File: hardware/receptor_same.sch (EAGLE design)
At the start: 62 parts, among them J1 ICSP, J2 SERIAL, J3 GPIO, J4 AUX-POWER, K1 HLS8L-DC5V, Q1 MMBT3904LT1G, U1 ATMEGA328P_TQFP, U2 SI4707, U3 TPA6111A2DR, U4 MCP16301/H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

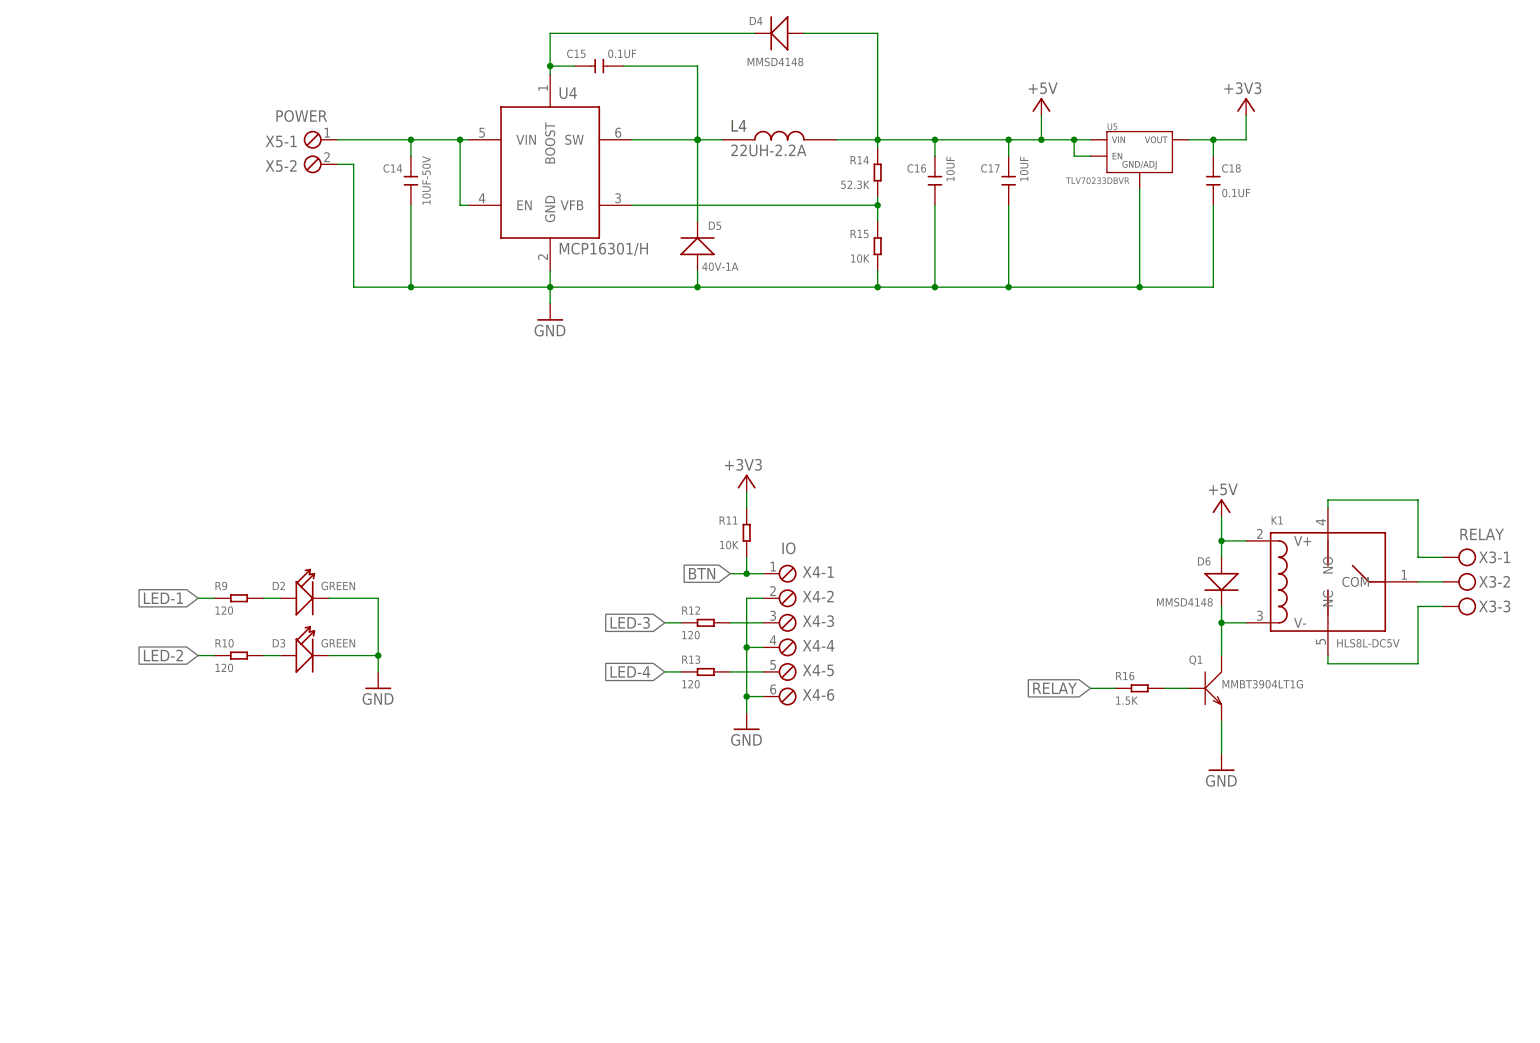
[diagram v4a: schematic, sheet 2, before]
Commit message: puntos de montaje en esquematico y pasa el erc
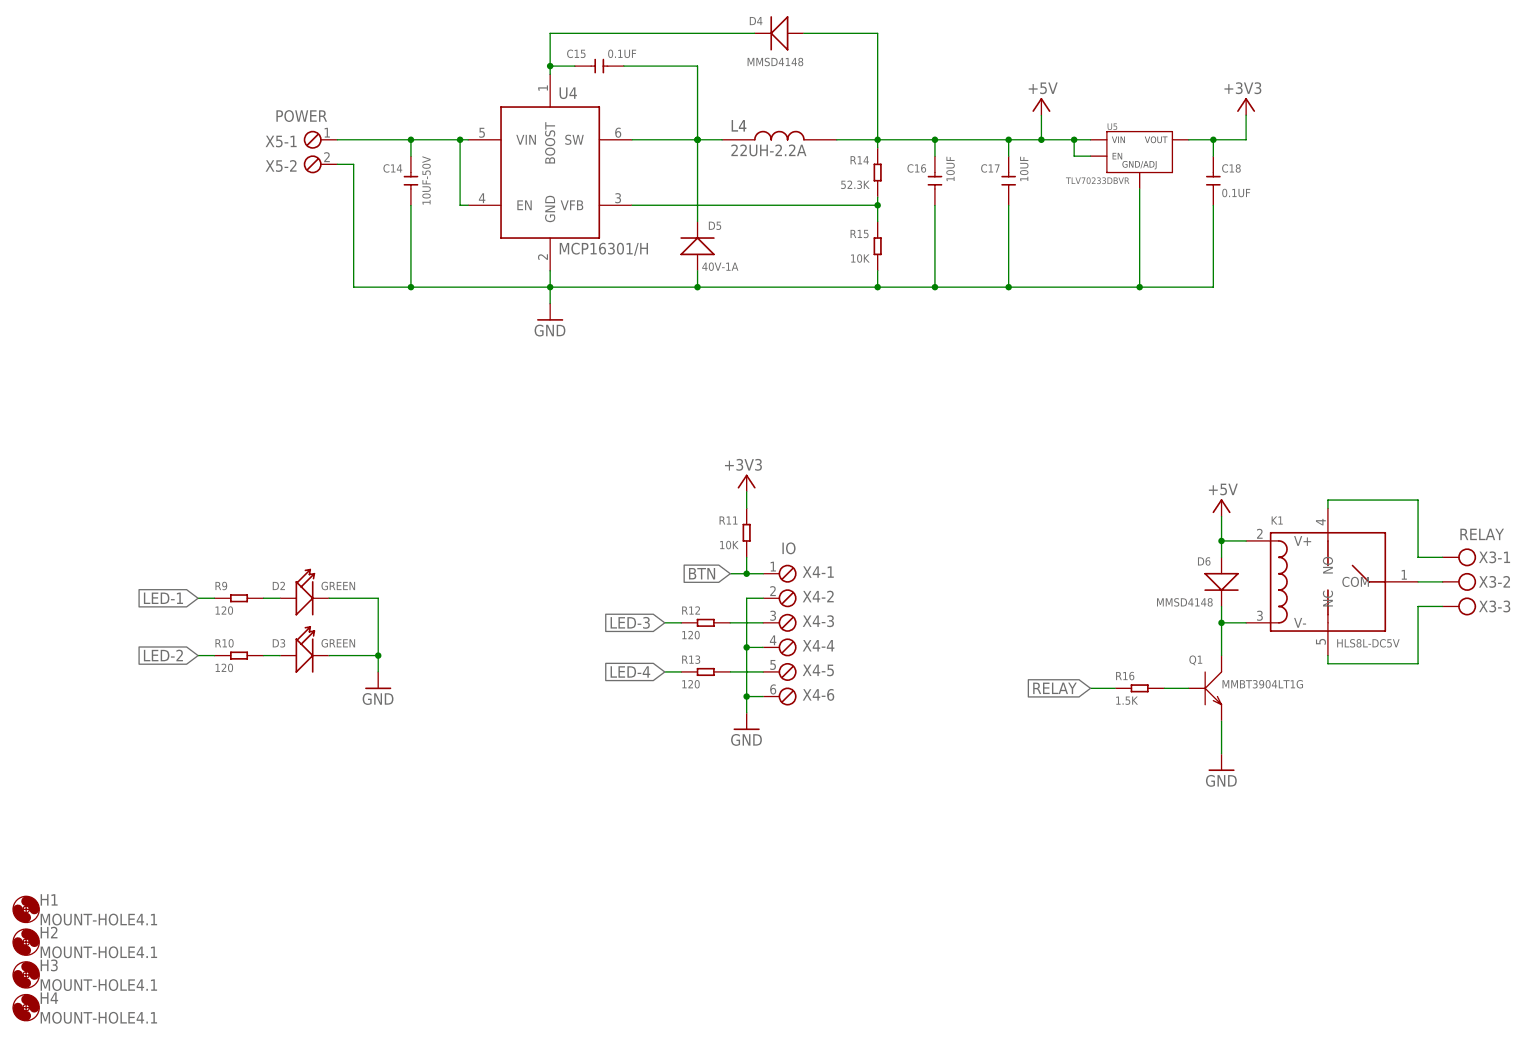
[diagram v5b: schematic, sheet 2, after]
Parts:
- added H1, H2, H3, H4: MOUNT-HOLE4.1, holes:MOUNT-HOLE4.1
- X1: value ANTENNA -> ANT
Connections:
- net N$23 renamed SW
- net N$25 renamed VIN
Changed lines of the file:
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@@
 </classes>
 <parts>
-<part name="FRAME1" library="frames" library_urn="urn:adsk.eagle:library:229" deviceset="A4L-LOC" device=""/>
+<part name="FRAME1" library="frames" library_urn="urn:adsk.eagle:library:229" deviceset="A4L-LOC" device="" value="SHEET-1"/>
 <part name="U1" library="SparkFun-IC-Microcontroller" library_urn="urn:adsk.eagle:library:525" deviceset="ATMEGA328P_TQFP" device="" package3d_urn="urn:adsk.eagle:package:38945/1" value="ATMEGA328P_TQFP">
 <attribute name="MPN" value="ATMEGA328P-AU"/>
@@
 <attribute name="SPICEPREFIX" value="G"/>
 </part>
-<part name="P+9" library="supply1" library_urn="urn:adsk.eagle:library:371" deviceset="VCC" device=""/>
 <part name="GND11" library="supply1" library_urn="urn:adsk.eagle:library:371" deviceset="GND" device="">
 <attribute name="SPICEPREFIX" value="G"/>
@@
 <part name="P+11" library="supply1" library_urn="urn:adsk.eagle:library:371" deviceset="+3V3" device=""/>
 <part name="GND17" library="supply1" library_urn="urn:adsk.eagle:library:371" deviceset="GND" device=""/>
-<part name="X1" library="con-phoenix-254" library_urn="urn:adsk.eagle:library:172" deviceset="MPT2" device="" package3d_urn="urn:adsk.eagle:package:9320/1" value="ANTENNA">
+<part name="X1" library="con-phoenix-254" library_urn="urn:adsk.eagle:library:172" deviceset="MPT2" device="" package3d_urn="urn:adsk.eagle:package:9320/1" value="ANT">
 <attribute name="MPN" value="1725656"/>
 </part>
@@
 <attribute name="MPN" value="RC0805JR-07120RL"/>
 </part>
-<part name="FRAME2" library="frames" library_urn="urn:adsk.eagle:library:229" deviceset="A4L-LOC" device=""/>
+<part name="FRAME2" library="frames" library_urn="urn:adsk.eagle:library:229" deviceset="A4L-LOC" device="" value="SHEET-2"/>
 <part name="K1" library="OPL_Relay" library_urn="urn:adsk.eagle:library:8004835" deviceset="RELAY-HLS8L-DC5V-S-C" device="HLS8L-DC5V-S-C" package3d_urn="urn:adsk.eagle:package:8004880/1" value="HLS8L-DC5V">
 <attribute name="MPN" value="HLS8L-DC5V-S-C"/>
@@
 <part name="P+19" library="supply1" library_urn="urn:adsk.eagle:library:371" deviceset="+3V3" device=""/>
 <part name="R15" library="OPL_Resistor" library_urn="urn:adsk.eagle:library:8004883" deviceset="SMD-RES-10K-5%-1/10W(0603)" device="" package3d_urn="urn:adsk.eagle:package:8004941/1" value="10K"/>
+<part name="H1" library="holes" library_urn="urn:adsk.eagle:library:237" deviceset="MOUNT-HOLE" device="4.1" package3d_urn="urn:adsk.eagle:package:14273/1"/>
+<part name="H2" library="holes" library_urn="urn:adsk.eagle:library:237" deviceset="MOUNT-HOLE" device="4.1" package3d_urn="urn:adsk.eagle:package:14273/1"/>
+<part name="H3" library="holes" library_urn="urn:adsk.eagle:library:237" deviceset="MOUNT-HOLE" device="4.1" package3d_urn="urn:adsk.eagle:package:14273/1"/>
+<part name="H4" library="holes" library_urn="urn:adsk.eagle:library:237" deviceset="MOUNT-HOLE" device="4.1" package3d_urn="urn:adsk.eagle:package:14273/1"/>
+<part name="P+20" library="supply1" library_urn="urn:adsk.eagle:library:371" deviceset="+3V3" device=""/>
 </parts>
 <sheets>
@@
 <attribute name="VALUE" x="220.98" y="106.68" size="1.778" layer="96"/>
 </instance>
-<instance part="P+9" gate="VCC" x="176.53" y="76.2" smashed="yes">
-<attribute name="VALUE" x="179.07" y="78.74" size="1.778" layer="96" rot="R180"/>
-</instance>
 <instance part="GND11" gate="1" x="176.53" y="49.53" smashed="yes">
 <attribute name="VALUE" x="173.99" y="46.99" size="1.778" layer="96"/>
@@
 <instance part="P+18" gate="1" x="58.42" y="123.19" smashed="yes">
 <attribute name="VALUE" x="60.96" y="125.73" size="1.778" layer="96" rot="R180"/>
+</instance>
+<instance part="P+20" gate="G$1" x="176.53" y="74.93" smashed="yes">
+<attribute name="VALUE" x="179.07" y="77.47" size="1.778" layer="96" rot="R180"/>
 </instance>
 </instances>
@@
 <pinref part="U3" gate="G$1" pin="VDD"/>
 <wire x1="179.07" y1="67.31" x2="176.53" y2="67.31" width="0.1524" layer="91"/>
-<pinref part="P+9" gate="VCC" pin="VCC"/>
-<wire x1="176.53" y1="67.31" x2="176.53" y2="73.66" width="0.1524" layer="91"/>
+<wire x1="176.53" y1="67.31" x2="176.53" y2="72.39" width="0.1524" layer="91"/>
+<pinref part="P+20" gate="G$1" pin="+3V3"/>
 </segment>
 <segment>
@@
 <attribute name="NAME" x="146.05" y="133.35" size="1.27" layer="95" ratio="10" rot="R180"/>
 <attribute name="VALUE" x="146.05" y="129.54" size="1.27" layer="96" ratio="10" rot="R180"/>
+</instance>
+<instance part="H1" gate="G$1" x="15.24" y="27.94" smashed="yes">
+<attribute name="NAME" x="17.272" y="28.5242" size="1.778" layer="95"/>
+<attribute name="VALUE" x="17.272" y="25.4762" size="1.778" layer="96"/>
+</instance>
+<instance part="H2" gate="G$1" x="15.24" y="22.86" smashed="yes">
+<attribute name="NAME" x="17.272" y="23.4442" size="1.778" layer="95"/>
+<attribute name="VALUE" x="17.272" y="20.3962" size="1.778" layer="96"/>
+</instance>
+<instance part="H3" gate="G$1" x="15.24" y="17.78" smashed="yes">
+<attribute name="NAME" x="17.272" y="18.3642" size="1.778" layer="95"/>
+<attribute name="VALUE" x="17.272" y="15.3162" size="1.778" layer="96"/>
+</instance>
+<instance part="H4" gate="G$1" x="15.24" y="12.7" smashed="yes">
+<attribute name="NAME" x="17.272" y="13.2842" size="1.778" layer="95"/>
+<attribute name="VALUE" x="17.272" y="10.2362" size="1.778" layer="96"/>
 </instance>
 </instances>
@@
 </segment>
 </net>
-<net name="N$25" class="0">
+<net name="VIN" class="0">
 <segment>
 <wire x1="83.82" y1="137.16" x2="82.55" y2="137.16" width="0.1524" layer="91"/>
@@
 </segment>
 </net>
-<net name="N$23" class="0">
-<segment>
-<wire x1="109.22" y1="147.32" x2="119.38" y2="147.32" width="0.1524" layer="91"/>
+<net name="SW" class="0">
+<segment>
 <wire x1="119.38" y1="147.32" x2="119.38" y2="158.75" width="0.1524" layer="91"/>
 <pinref part="C15" gate="G$1" pin="1"/>
@@
 <wire x1="119.38" y1="147.32" x2="123.19" y2="147.32" width="0.1524" layer="91"/>
 <junction x="119.38" y="147.32"/>
+<wire x1="119.38" y1="134.62" x2="119.38" y2="147.32" width="0.1524" layer="91"/>
 <pinref part="U4" gate="G$1" pin="SW"/>
-<wire x1="119.38" y1="134.62" x2="119.38" y2="147.32" width="0.1524" layer="91"/>
-</segment>
-</net>
+<wire x1="119.38" y1="147.32" x2="109.22" y2="147.32" width="0.1524" layer="91"/>
+</segment>
+</net>

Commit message: avances ruteo si + amp
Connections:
- net N$11: now also C10.+; no longer C9.+
- net N$13: now also C9.+; no longer C10.+
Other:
- moved on the sheet: C10, C9, L2, L3, X2-1, X2-2, X2-3
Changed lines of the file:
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@@
 <setting verticaltext="up"/>
 </settings>
-<grid distance="0.1" unitdist="inch" unit="inch" style="lines" multiple="1" display="no" altdistance="0.01" altunitdist="inch" altunit="inch"/>
+<grid distance="0.05" unitdist="inch" unit="inch" style="lines" multiple="1" display="no" altdistance="0.01" altunitdist="inch" altunit="inch"/>
 <layers>
 <layer number="1" name="Top" color="4" fill="1" visible="no" active="no"/>
@@
 <attribute name="VALUE" x="181.61" y="83.82" size="1.27" layer="96" ratio="10"/>
 </instance>
-<instance part="C9" gate="G$1" x="212.09" y="69.85" smashed="yes" rot="R90">
-<attribute name="NAME" x="211.455" y="72.136" size="1.778" layer="95" font="vector" rot="R180"/>
-<attribute name="VALUE" x="220.091" y="68.326" size="1.778" layer="96" font="vector" rot="R180"/>
-<attribute name="MPN" x="212.09" y="69.85" size="1.778" layer="96" rot="R90" display="off"/>
-</instance>
-<instance part="C10" gate="G$1" x="212.09" y="62.23" smashed="yes" rot="R90">
-<attribute name="NAME" x="211.455" y="64.516" size="1.778" layer="95" font="vector" rot="R180"/>
-<attribute name="VALUE" x="220.091" y="60.706" size="1.778" layer="96" font="vector" rot="R180"/>
-<attribute name="MPN" x="212.09" y="62.23" size="1.778" layer="96" rot="R90" display="off"/>
-</instance>
-<instance part="L2" gate="L" x="226.06" y="69.85" smashed="yes">
-<attribute name="NAME" x="223.52" y="71.12" size="1.27" layer="95" ratio="10"/>
-<attribute name="VALUE" x="223.52" y="67.31" size="1.27" layer="96" ratio="10"/>
-</instance>
-<instance part="L3" gate="L" x="226.06" y="62.23" smashed="yes">
-<attribute name="NAME" x="223.52" y="63.5" size="1.27" layer="95" ratio="10"/>
-<attribute name="VALUE" x="223.52" y="59.69" size="1.27" layer="96" ratio="10"/>
+<instance part="C9" gate="G$1" x="210.82" y="76.2" smashed="yes" rot="R90">
+<attribute name="NAME" x="210.185" y="78.486" size="1.778" layer="95" font="vector" rot="R180"/>
+<attribute name="VALUE" x="218.821" y="74.676" size="1.778" layer="96" font="vector" rot="R180"/>
+<attribute name="MPN" x="210.82" y="76.2" size="1.778" layer="96" rot="R90" display="off"/>
+</instance>
+<instance part="C10" gate="G$1" x="210.82" y="68.58" smashed="yes" rot="R90">
+<attribute name="NAME" x="210.185" y="70.866" size="1.778" layer="95" font="vector" rot="R180"/>
+<attribute name="VALUE" x="218.821" y="67.056" size="1.778" layer="96" font="vector" rot="R180"/>
+<attribute name="MPN" x="210.82" y="68.58" size="1.778" layer="96" rot="R90" display="off"/>
+</instance>
+<instance part="L2" gate="L" x="224.79" y="76.2" smashed="yes">
+<attribute name="NAME" x="222.25" y="77.47" size="1.27" layer="95" ratio="10"/>
+<attribute name="VALUE" x="222.25" y="73.66" size="1.27" layer="96" ratio="10"/>
+</instance>
+<instance part="L3" gate="L" x="224.79" y="68.58" smashed="yes">
+<attribute name="NAME" x="222.25" y="69.85" size="1.27" layer="95" ratio="10"/>
+<attribute name="VALUE" x="222.25" y="66.04" size="1.27" layer="96" ratio="10"/>
 </instance>
 <instance part="C11" gate="G$1" x="201.93" y="50.8" smashed="yes" rot="R270">
@@
 <attribute name="VALUE" x="199.39" y="39.37" size="1.778" layer="96"/>
 </instance>
-<instance part="GND13" gate="1" x="237.49" y="57.15" smashed="yes">
-<attribute name="VALUE" x="234.95" y="54.61" size="1.778" layer="96"/>
+<instance part="GND13" gate="1" x="236.22" y="63.5" smashed="yes">
+<attribute name="VALUE" x="233.68" y="60.96" size="1.778" layer="96"/>
 </instance>
 <instance part="C12" gate="G$1" x="189.23" y="39.37" smashed="yes" rot="R270">
@@
 <attribute name="VALUE" x="241.554" y="133.858" size="1.778" layer="96"/>
 </instance>
-<instance part="X2" gate="-1" x="242.57" y="69.85" smashed="yes">
-<attribute name="NAME" x="246.126" y="69.215" size="1.778" layer="95"/>
-</instance>
-<instance part="X2" gate="-2" x="242.57" y="66.04" smashed="yes">
-<attribute name="NAME" x="246.126" y="65.405" size="1.778" layer="95"/>
-</instance>
-<instance part="X2" gate="-3" x="242.57" y="62.23" smashed="yes">
-<attribute name="NAME" x="246.126" y="61.595" size="1.778" layer="95"/>
-<attribute name="VALUE" x="242.824" y="72.898" size="1.778" layer="96"/>
+<instance part="X2" gate="-1" x="241.3" y="76.2" smashed="yes">
+<attribute name="NAME" x="244.856" y="75.565" size="1.778" layer="95"/>
+</instance>
+<instance part="X2" gate="-2" x="241.3" y="72.39" smashed="yes">
+<attribute name="NAME" x="244.856" y="71.755" size="1.778" layer="95"/>
+</instance>
+<instance part="X2" gate="-3" x="241.3" y="68.58" smashed="yes">
+<attribute name="NAME" x="244.856" y="67.945" size="1.778" layer="95"/>
+<attribute name="VALUE" x="241.554" y="79.248" size="1.778" layer="96"/>
 </instance>
 <instance part="P+12" gate="G$1" x="72.39" y="162.56" smashed="yes">
@@
 </segment>
 <segment>
-<wire x1="240.03" y1="66.04" x2="237.49" y2="66.04" width="0.1524" layer="91"/>
+<wire x1="238.76" y1="72.39" x2="236.22" y2="72.39" width="0.1524" layer="91"/>
 <pinref part="GND13" gate="1" pin="GND"/>
-<wire x1="237.49" y1="66.04" x2="237.49" y2="59.69" width="0.1524" layer="91"/>
+<wire x1="236.22" y1="72.39" x2="236.22" y2="66.04" width="0.1524" layer="91"/>
 <pinref part="X2" gate="-2" pin="1"/>
 </segment>
@@
 <pinref part="R7" gate="G$1" pin="2"/>
 <wire x1="199.39" y1="81.28" x2="201.93" y2="81.28" width="0.1524" layer="91"/>
-<wire x1="201.93" y1="81.28" x2="201.93" y2="69.85" width="0.1524" layer="91"/>
-<wire x1="201.93" y1="69.85" x2="209.55" y2="69.85" width="0.1524" layer="91"/>
-<pinref part="C9" gate="G$1" pin="+"/>
+<wire x1="201.93" y1="81.28" x2="201.93" y2="68.58" width="0.1524" layer="91"/>
 <pinref part="U3" gate="G$1" pin="VO1"/>
+<wire x1="201.93" y1="68.58" x2="201.93" y2="64.77" width="0.1524" layer="91"/>
 <wire x1="199.39" y1="64.77" x2="201.93" y2="64.77" width="0.1524" layer="91"/>
-<wire x1="201.93" y1="64.77" x2="201.93" y2="69.85" width="0.1524" layer="91"/>
-<junction x="201.93" y="69.85"/>
+<pinref part="C10" gate="G$1" pin="+"/>
+<wire x1="208.28" y1="68.58" x2="201.93" y2="68.58" width="0.1524" layer="91"/>
+<junction x="201.93" y="68.58"/>
 </segment>
 </net>
@@
 <pinref part="U3" gate="G$1" pin="VO2"/>
 <wire x1="199.39" y1="62.23" x2="204.47" y2="62.23" width="0.1524" layer="91"/>
-<pinref part="C10" gate="G$1" pin="+"/>
-<wire x1="204.47" y1="62.23" x2="209.55" y2="62.23" width="0.1524" layer="91"/>
 <pinref part="R8" gate="G$1" pin="2"/>
 <wire x1="189.23" y1="86.36" x2="204.47" y2="86.36" width="0.1524" layer="91"/>
-<wire x1="204.47" y1="86.36" x2="204.47" y2="62.23" width="0.1524" layer="91"/>
-<junction x="204.47" y="62.23"/>
+<wire x1="204.47" y1="86.36" x2="204.47" y2="76.2" width="0.1524" layer="91"/>
+<pinref part="C9" gate="G$1" pin="+"/>
+<wire x1="204.47" y1="76.2" x2="204.47" y2="62.23" width="0.1524" layer="91"/>
+<wire x1="208.28" y1="76.2" x2="204.47" y2="76.2" width="0.1524" layer="91"/>
+<junction x="204.47" y="76.2"/>
 </segment>
 </net>
@@
 <pinref part="C9" gate="G$1" pin="-"/>
 <pinref part="L2" gate="L" pin="1"/>
-<wire x1="217.17" y1="69.85" x2="220.98" y2="69.85" width="0.1524" layer="91"/>
+<wire x1="215.9" y1="76.2" x2="219.71" y2="76.2" width="0.1524" layer="91"/>
 </segment>
 </net>
@@
 <segment>
 <pinref part="L2" gate="L" pin="2"/>
-<wire x1="231.14" y1="69.85" x2="240.03" y2="69.85" width="0.1524" layer="91"/>
+<wire x1="229.87" y1="76.2" x2="238.76" y2="76.2" width="0.1524" layer="91"/>
 <pinref part="X2" gate="-1" pin="1"/>
 </segment>
@@
 <segment>
 <pinref part="L3" gate="L" pin="2"/>
-<wire x1="240.03" y1="62.23" x2="231.14" y2="62.23" width="0.1524" layer="91"/>
+<wire x1="238.76" y1="68.58" x2="229.87" y2="68.58" width="0.1524" layer="91"/>
 <pinref part="X2" gate="-3" pin="1"/>
 </segment>
@@
 <segment>
 <pinref part="L3" gate="L" pin="1"/>
-<wire x1="220.98" y1="62.23" x2="217.17" y2="62.23" width="0.1524" layer="91"/>
+<wire x1="219.71" y1="68.58" x2="215.9" y2="68.58" width="0.1524" layer="91"/>
 <pinref part="C10" gate="G$1" pin="-"/>
 </segment>

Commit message: avances pcba
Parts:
- X1: value ANT -> ANTENNA
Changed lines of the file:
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@@
 <setting verticaltext="up"/>
 </settings>
-<grid distance="0.05" unitdist="inch" unit="inch" style="lines" multiple="1" display="no" altdistance="0.01" altunitdist="inch" altunit="inch"/>
+<grid distance="0.1" unitdist="inch" unit="inch" style="lines" multiple="1" display="no" altdistance="0.01" altunitdist="inch" altunit="inch"/>
 <layers>
 <layer number="1" name="Top" color="4" fill="1" visible="no" active="no"/>
@@
 <part name="P+11" library="supply1" library_urn="urn:adsk.eagle:library:371" deviceset="+3V3" device=""/>
 <part name="GND17" library="supply1" library_urn="urn:adsk.eagle:library:371" deviceset="GND" device=""/>
-<part name="X1" library="con-phoenix-254" library_urn="urn:adsk.eagle:library:172" deviceset="MPT2" device="" package3d_urn="urn:adsk.eagle:package:9320/1" value="ANT">
+<part name="X1" library="con-phoenix-254" library_urn="urn:adsk.eagle:library:172" deviceset="MPT2" device="" package3d_urn="urn:adsk.eagle:package:9320/1" value="ANTENNA">
 <attribute name="MPN" value="1725656"/>
 </part>

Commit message: pcb terminado
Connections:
- net N$15 renamed L
- net N$16 renamed R
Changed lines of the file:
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@@
 </segment>
 </net>
-<net name="N$15" class="0">
+<net name="L" class="0">
 <segment>
 <pinref part="L2" gate="L" pin="2"/>
@@
 </segment>
 </net>
-<net name="N$16" class="0">
+<net name="R" class="0">
 <segment>
 <pinref part="L3" gate="L" pin="2"/>
